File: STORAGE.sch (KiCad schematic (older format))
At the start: 10 parts

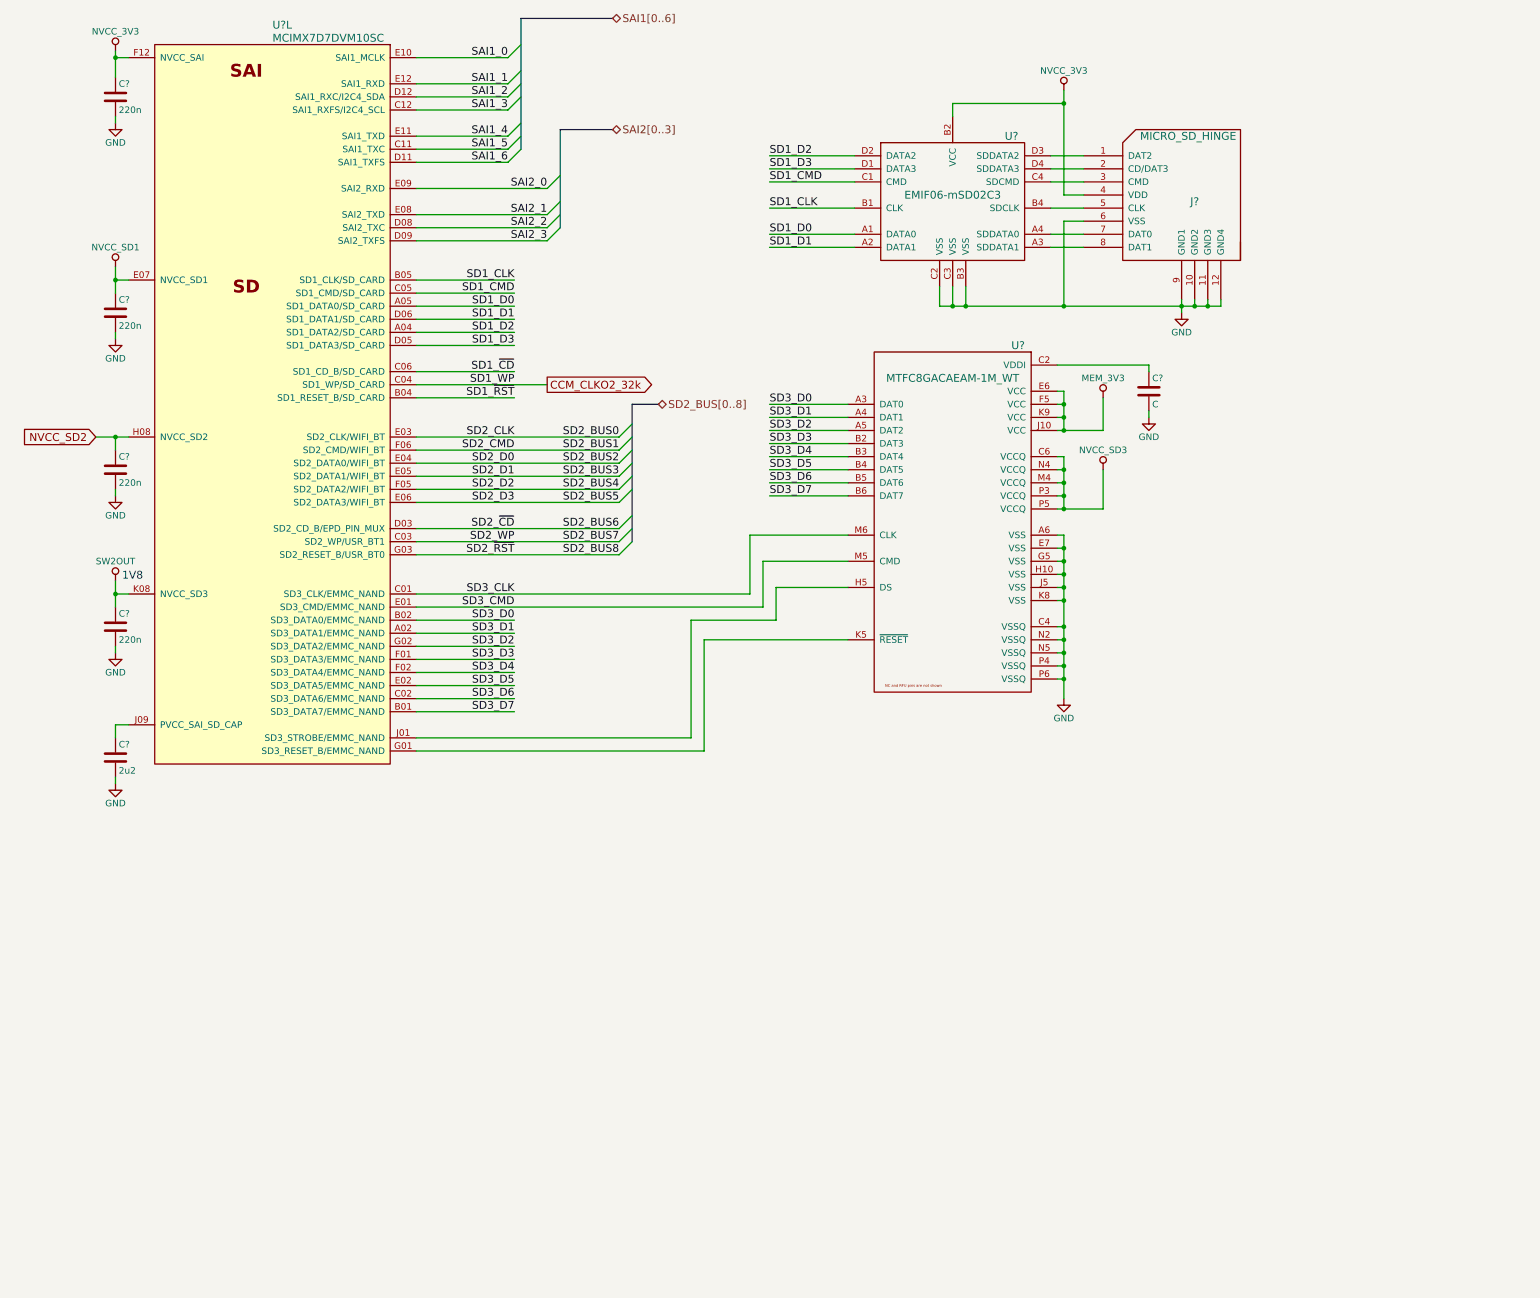
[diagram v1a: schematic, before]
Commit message: Prepare for two battery types NiMH battery for using the original battery pack LiPo battery for using long lasting modern battery
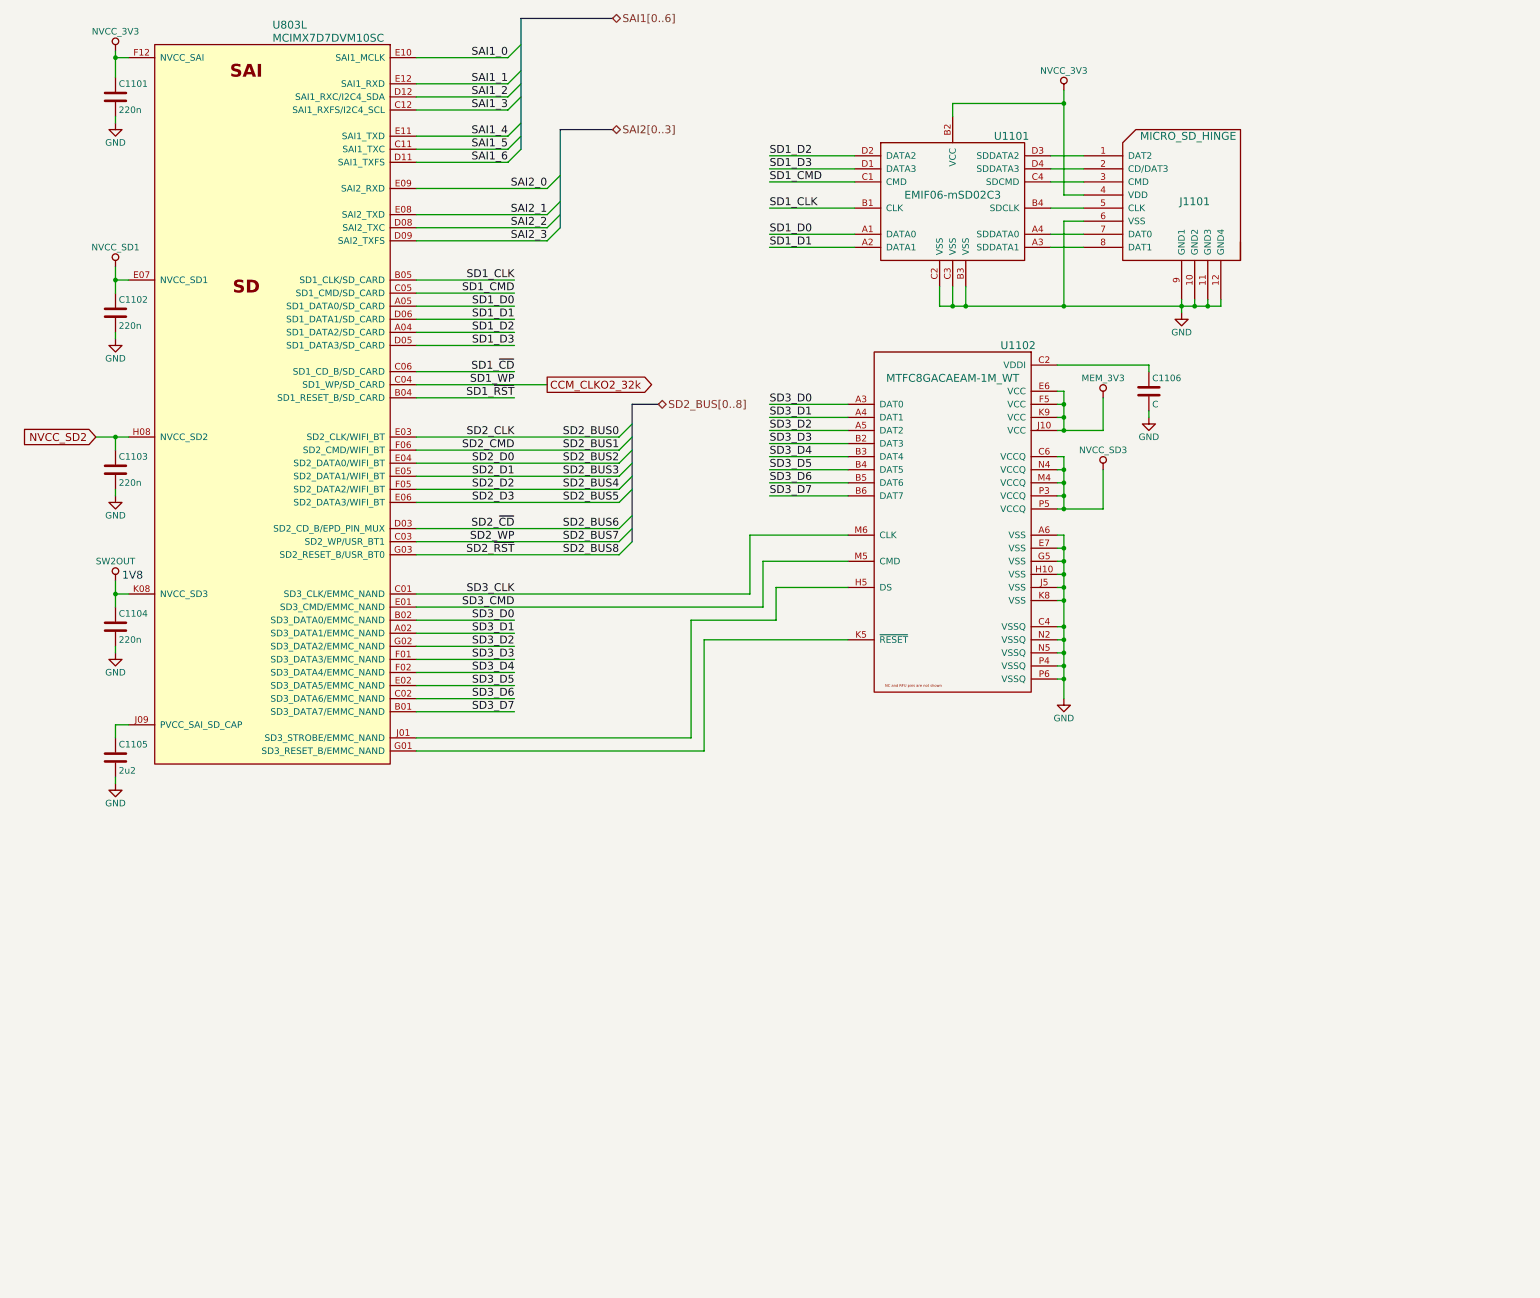
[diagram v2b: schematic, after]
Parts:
- gave numbers to parts that had none: 10
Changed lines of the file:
@@
 EESchema Schematic File Version 2
-LIBS:3210retro-rescue
-LIBS:power
-LIBS:device
-LIBS:transistors
-LIBS:conn
-LIBS:linear
-LIBS:regul
-LIBS:74xx
-LIBS:cmos4000
-LIBS:adc-dac
-LIBS:memory
-LIBS:xilinx
-LIBS:microcontrollers
-LIBS:dsp
-LIBS:microchip
-LIBS:analog_switches
-LIBS:motorola
-LIBS:texas
-LIBS:intel
-LIBS:audio
-LIBS:interface
-LIBS:digital-audio
-LIBS:philips
-LIBS:display
-LIBS:cypress
-LIBS:siliconi
-LIBS:opto
-LIBS:atmel
-LIBS:contrib
-LIBS:valves
 LIBS:a7
 LIBS:ft232rl
@@
 LIBS:sn74avc2t244
 LIBS:lsm9ds1
+LIBS:WM8960CGEFL
+LIBS:tps61021a
+LIBS:bq24400
+LIBS:power
+LIBS:device
+LIBS:transistors
+LIBS:conn
+LIBS:linear
+LIBS:regul
+LIBS:74xx
+LIBS:cmos4000
+LIBS:adc-dac
+LIBS:memory
+LIBS:xilinx
+LIBS:microcontrollers
+LIBS:dsp
+LIBS:microchip
+LIBS:analog_switches
+LIBS:motorola
+LIBS:texas
+LIBS:intel
+LIBS:audio
+LIBS:interface
+LIBS:digital-audio
+LIBS:philips
+LIBS:display
+LIBS:cypress
+LIBS:siliconi
+LIBS:opto
+LIBS:atmel
+LIBS:contrib
+LIBS:valves
 LIBS:3210retro-cache
 EELAYER 25 0
@@
 $EndDescr
 $Comp
-L MCIMX7D7DVM10SC U?
+L MCIMX7D7DVM10SC U803
 U 12 1 594351FC
 P 3050 950
-F 0 "U?" H 3050 950 60  0000 L CNN
+F 0 "U803" H 3050 950 60  0000 L CNN
 F 1 "MCIMX7D7DVM10SC" H 3050 850 60  0000 L CNN
 F 2 "" H 800 2650 60  0001 C CNN
@@
 SAI2[0..3]
 $Comp
-L MICRO_SD_HINGE J?
+L MICRO_SD_HINGE J1101
 U 1 1 5944B602
 P 10050 2350
-F 0 "J?" H 10100 2400 60  0000 C CNN
+F 0 "J1101" H 10100 2400 60  0000 C CNN
 F 1 "MICRO_SD_HINGE" H 10050 2900 60  0000 C CNN
 F 2 "" V 10160 1850 60  0000 C CNN
@@
 $EndComp
 $Comp
-L GND #PWR?
+L GND #PWR1114
 U 1 1 5944B647
 P 10000 3150
-F 0 "#PWR?" H 10000 2900 50  0001 C CNN
+F 0 "#PWR1114" H 10000 2900 50  0001 C CNN
 F 1 "GND" H 10000 3000 50  0000 C CNN
 F 2 "" H 10000 3150 50  0000 C CNN
@@
 	9000 1950 9250 1950
 $Comp
-L EMIF06-mSD02C3 U?
+L EMIF06-mSD02C3 U1101
 U 1 1 5944C05B
 P 8250 2250
-F 0 "U?" H 8700 2700 60  0000 C CNN
+F 0 "U1101" H 8700 2700 60  0000 C CNN
 F 1 "EMIF06-mSD02C3" H 8250 2250 60  0000 C CNN
 F 2 "" H 8700 2700 60  0001 C CNN
@@
 $EndComp
 $Comp
-L NVCC_3V3 #PWR?
+L NVCC_3V3 #PWR1109
 U 1 1 5944C8E9
 P 9100 1450
-F 0 "#PWR?" H 9100 1300 50  0001 C CNN
+F 0 "#PWR1109" H 9100 1300 50  0001 C CNN
 F 1 "NVCC_3V3" H 9100 1600 50  0000 C CNN
 F 2 "" H 9100 1450 50  0001 C CNN
@@
 SD3_D7
 $Comp
-L C C?
+L C C1106
 U 1 1 5944DAED
 P 9750 3750
-F 0 "C?" H 9775 3850 50  0000 L CNN
+F 0 "C1106" H 9775 3850 50  0000 L CNN
 F 1 "C" H 9775 3650 50  0000 L CNN
 F 2 "" H 9788 3600 50  0000 C CNN
@@
 	9750 3550 9050 3550
 $Comp
-L GND #PWR?
+L GND #PWR1113
 U 1 1 5944DCC6
 P 9750 3950
-F 0 "#PWR?" H 9750 3700 50  0001 C CNN
+F 0 "#PWR1113" H 9750 3700 50  0001 C CNN
 F 1 "GND" H 9750 3800 50  0000 C CNN
 F 2 "" H 9750 3950 50  0000 C CNN
@@
 	9750 3950 9750 3900
 $Comp
-L MEM_3V3 #PWR?
+L MEM_3V3 #PWR1111
 U 1 1 5944DD41
 P 9400 3800
-F 0 "#PWR?" H 9400 3650 50  0001 C CNN
+F 0 "#PWR1111" H 9400 3650 50  0001 C CNN
 F 1 "MEM_3V3" H 9400 3950 50  0000 C CNN
 F 2 "" H 9400 3800 50  0001 C CNN
@@
 Connection ~ 9100 3950
 $Comp
-L MTFC8GACAEAM-1M_WT U?
+L MTFC8GACAEAM-1M_WT U1102
 U 1 1 5944D61A
 P 8250 3650
-F 0 "U?" H 8750 3900 60  0000 C CNN
+F 0 "U1102" H 8750 3900 60  0000 C CNN
 F 1 "MTFC8GACAEAM-1M_WT" H 8250 3650 60  0000 C CNN
 F 2 "" H 9050 3900 60  0001 C CNN
@@
 Connection ~ 9100 4650
 $Comp
-L NVCC_SD3 #PWR?
+L NVCC_SD3 #PWR1112
 U 1 1 5944E338
 P 9400 4350
-F 0 "#PWR?" H 9400 4200 50  0001 C CNN
+F 0 "#PWR1112" H 9400 4200 50  0001 C CNN
 F 1 "NVCC_SD3" H 9400 4500 50  0000 C CNN
 F 2 "" H 9400 4350 50  0001 C CNN
@@
 	9050 5950 9100 5950
 $Comp
-L GND #PWR?
+L GND #PWR1110
 U 1 1 5944E514
 P 9100 6100
-F 0 "#PWR?" H 9100 5850 50  0001 C CNN
+F 0 "#PWR1110" H 9100 5850 50  0001 C CNN
 F 1 "GND" H 9100 5950 50  0000 C CNN
 F 2 "" H 9100 6100 50  0000 C CNN
@@
 $EndComp
 $Comp
-L C C?
+L C C1101
 U 1 1 5944EE67
 P 1850 1500
-F 0 "C?" H 1875 1600 50  0000 L CNN
+F 0 "C1101" H 1875 1600 50  0000 L CNN
 F 1 "220n" H 1875 1400 50  0000 L CNN
 F 2 "" H 1888 1350 50  0000 C CNN
@@
 	1850 1150 1850 1350
 $Comp
-L NVCC_3V3 #PWR?
+L NVCC_3V3 #PWR1101
 U 1 1 5944EF86
 P 1850 1150
-F 0 "#PWR?" H 1850 1000 50  0001 C CNN
+F 0 "#PWR1101" H 1850 1000 50  0001 C CNN
 F 1 "NVCC_3V3" H 1850 1300 50  0000 C CNN
 F 2 "" H 1850 1150 50  0001 C CNN
@@
 Connection ~ 1850 1200
 $Comp
-L GND #PWR?
+L GND #PWR1102
 U 1 1 5944F032
 P 1850 1700
-F 0 "#PWR?" H 1850 1450 50  0001 C CNN
+F 0 "#PWR1102" H 1850 1450 50  0001 C CNN
 F 1 "GND" H 1850 1550 50  0000 C CNN
 F 2 "" H 1850 1700 50  0000 C CNN
@@
 	1850 1700 1850 1650
 $Comp
-L C C?
+L C C1103
 U 1 1 5944F9F5
 P 1850 4350
-F 0 "C?" H 1875 4450 50  0000 L CNN
+F 0 "C1103" H 1875 4450 50  0000 L CNN
 F 1 "220n" H 1875 4250 50  0000 L CNN
 F 2 "" H 1888 4200 50  0000 C CNN
@@
 	1850 4100 1850 4200
 $Comp
-L GND #PWR?
+L GND #PWR1105
 U 1 1 5944F9FC
 P 1850 4550
-F 0 "#PWR?" H 1850 4300 50  0001 C CNN
+F 0 "#PWR1105" H 1850 4300 50  0001 C CNN
 F 1 "GND" H 1850 4400 50  0000 C CNN
 F 2 "" H 1850 4550 50  0000 C CNN
@@
 	1850 4550 1850 4500
 $Comp
-L C C?
+L C C1102
 U 1 1 5944FAB3
 P 1850 3150
-F 0 "C?" H 1875 3250 50  0000 L CNN
+F 0 "C1102" H 1875 3250 50  0000 L CNN
 F 1 "220n" H 1875 3050 50  0000 L CNN
 F 2 "" H 1888 3000 50  0000 C CNN
@@
 	1850 2800 1850 3000
 $Comp
-L GND #PWR?
+L GND #PWR1104
 U 1 1 5944FABA
 P 1850 3350
-F 0 "#PWR?" H 1850 3100 50  0001 C CNN
+F 0 "#PWR1104" H 1850 3100 50  0001 C CNN
 F 1 "GND" H 1850 3200 50  0000 C CNN
 F 2 "" H 1850 3350 50  0000 C CNN
@@
 	1850 3350 1850 3300
 $Comp
-L C C?
+L C C1104
 U 1 1 5944FB0D
 P 1850 5550
-F 0 "C?" H 1875 5650 50  0000 L CNN
+F 0 "C1104" H 1875 5650 50  0000 L CNN
 F 1 "220n" H 1875 5450 50  0000 L CNN
 F 2 "" H 1888 5400 50  0000 C CNN
@@
 	1850 5200 1850 5400
 $Comp
-L GND #PWR?
+L GND #PWR1107
 U 1 1 5944FB14
 P 1850 5750
-F 0 "#PWR?" H 1850 5500 50  0001 C CNN
+F 0 "#PWR1107" H 1850 5500 50  0001 C CNN
 F 1 "GND" H 1850 5600 50  0000 C CNN
 F 2 "" H 1850 5750 50  0000 C CNN
@@
 	1850 5750 1850 5700
 $Comp
-L C C?
+L C C1105
 U 1 1 5944FB38
 P 1850 6550
-F 0 "C?" H 1875 6650 50  0000 L CNN
+F 0 "C1105" H 1875 6650 50  0000 L CNN
 F 1 "2u2" H 1875 6450 50  0000 L CNN
 F 2 "" H 1888 6400 50  0000 C CNN
@@
 	1850 6300 1850 6400
 $Comp
-L GND #PWR?
+L GND #PWR1108
 U 1 1 5944FC97
 P 1850 6750
-F 0 "#PWR?" H 1850 6500 50  0001 C CNN
+F 0 "#PWR1108" H 1850 6500 50  0001 C CNN
 F 1 "GND" H 1850 6600 50  0000 C CNN
 F 2 "" H 1850 6750 50  0000 C CNN
@@
 Connection ~ 1850 2900
 $Comp
-L SW2OUT #PWR?
+L SW2OUT #PWR1106
 U 1 1 5944FEB5
 P 1850 5200
-F 0 "#PWR?" H 1850 5050 50  0001 C CNN
+F 0 "#PWR1106" H 1850 5050 50  0001 C CNN
 F 1 "SW2OUT" H 1850 5350 50  0000 C CNN
 F 2 "" H 1850 5200 50  0001 C CNN
@@
 1V8
 $Comp
-L NVCC_SD1 #PWR?
+L NVCC_SD1 #PWR1103
 U 1 1 594500AD
 P 1850 2800
-F 0 "#PWR?" H 1850 2650 50  0001 C CNN
+F 0 "#PWR1103" H 1850 2650 50  0001 C CNN
 F 1 "NVCC_SD1" H 1850 2950 50  0000 C CNN
 F 2 "" H 1850 2800 50  0001 C CNN
